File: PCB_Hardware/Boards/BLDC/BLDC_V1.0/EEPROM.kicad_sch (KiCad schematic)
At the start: 4 parts, among them U16 CAT24C256

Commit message: Add DBcan transport refactor, BLDC V1.0 schematic + sim work, HAL submodule
- DBcan: replace bare-register driver with vendor-agnostic transport abstraction (core/, transports/, refactored bootloader driver, README)
- Add stm32g4xx_hal_driver as Firmware/libs submodule
- Add HAL config for BLDC board (stm32g4xx_hal_conf.h)
- BLDC V1.0: schematic edits across 10 sheets (footprint assignments, repositioning); design-doc README (gate-driver constraints, FET selection / TPH3R70APL, thermal analysis)
- ngspice simulation workflow (cap sweeps, half-bridge slow turn-on)
- Ignore .obsidian/ vault state and large simulation CSV exports
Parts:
- C46: footprint (none) -> Capacitor_SMD:C_0402_1005Metric
- R27, R28: footprint (none) -> Resistor_SMD:R_0402_1005Metric
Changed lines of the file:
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@@
 			)
 		)
-		(property "Footprint" ""
+		(property "Footprint" "Resistor_SMD:R_0402_1005Metric"
 			(at 137.922 88.9 90)
 			(hide yes)
@@
 			)
 		)
-		(property "Footprint" ""
+		(property "Footprint" "Capacitor_SMD:C_0402_1005Metric"
 			(at 152.0952 92.71 0)
 			(hide yes)
@@
 			)
 		)
-		(property "Footprint" ""
+		(property "Footprint" "Resistor_SMD:R_0402_1005Metric"
 			(at 127.762 88.9 90)
 			(hide yes)

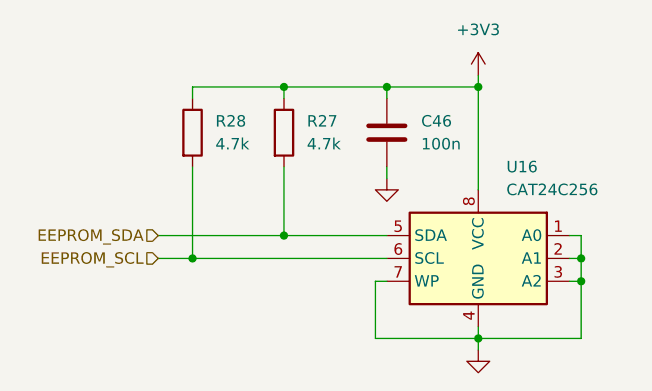
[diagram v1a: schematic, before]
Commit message: Created organization around the symbol lib and did a first pass layout of the BDLC
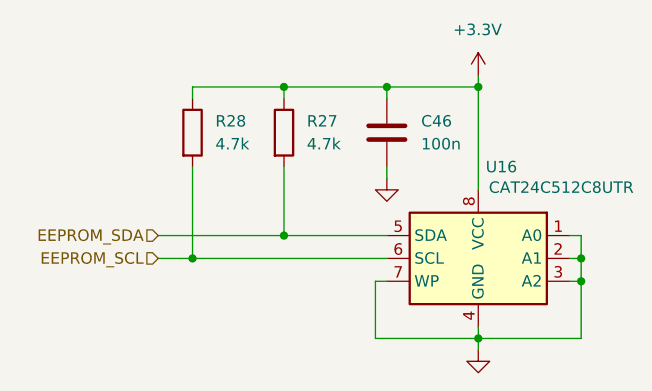
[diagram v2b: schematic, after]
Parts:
- U16: value CAT24C256 -> CAT24C512C8UTR; footprint (none) -> DBRobot:CAT24C512C8UTR
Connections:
- net +3V3 renamed +3.3V
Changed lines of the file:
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@@
-	)
-	(symbol
-		(lib_id "Memory_EEPROM:CAT24C256")
-		(at 161.29 102.87 0)
-		(mirror y)
-		(unit 1)
-		(body_style 1)
-		(exclude_from_sim no)
-		(in_bom yes)
-		(on_board yes)
-		(in_pos_files yes)
-		(dnp no)
-		(fields_autoplaced yes)
-		(property "Reference" "U16"
-			(at 164.4081 92.71 0)
-			(show_name no)
-			(do_not_autoplace no)
-			(effects
-				(font
-					(size 1.27 1.27)
-				)
-				(justify right)
-			)
-		)
-		(property "Value" "CAT24C256"
-			(at 164.4081 95.25 0)
-			(show_name no)
-			(do_not_autoplace no)
-			(effects
-				(font
-					(size 1.27 1.27)
-				)
-				(justify right)
-			)
-		)
-		(property "Footprint" ""
-			(at 161.29 102.87 0)
-			(hide yes)
-			(show_name no)
-			(do_not_autoplace no)
-			(effects
-				(font
-					(size 1.27 1.27)
-				)
-			)
-		)
-		(property "Datasheet" "https://www.onsemi.cn/PowerSolutions/document/CAT24C256-D.PDF"
-			(at 161.29 102.87 0)
-			(hide yes)
-			(show_name no)
-			(do_not_autoplace no)
-			(effects
-				(font
-					(size 1.27 1.27)
-				)
-			)
-		)
-		(property "Description" "256 kb CMOS Serial EEPROM, DIP-8/SOIC-8/TSSOP-8/DFN-8"
-			(at 161.29 102.87 0)
-			(hide yes)
-			(show_name no)
-			(do_not_autoplace no)
-			(effects
-				(font
-					(size 1.27 1.27)
-				)
-			)
-		)
-		(pin "3"
-		)
-		(pin "6"
-		)
-		(pin "1"
-		)
-		(pin "7"
-		)
-		(pin "5"
-		)
-		(pin "2"
-		)
-		(pin "4"
-		)
-		(pin "8"
-		)
-		(instances
-			(project "BLDC_V1.0"
-				(path "/55f9ea03-7b89-4b61-9599-7cac20295fbb/8c82480a-69eb-4e57-815e-68aa86fb6e72"
-					(reference "U16")
-					(unit 1)
-				)
-			)
-		)
 	)
 	(symbol
@@
 	)
 	(symbol
+		(lib_id "Memory_EEPROM:CAT24C256")
+		(at 161.29 102.87 0)
+		(mirror y)
+		(unit 1)
+		(body_style 1)
+		(exclude_from_sim no)
+		(in_bom yes)
+		(on_board yes)
+		(in_pos_files yes)
+		(dnp no)
+		(property "Reference" "U16"
+			(at 165.608 92.71 0)
+			(show_name no)
+			(do_not_autoplace no)
+			(effects
+				(font
+					(size 1.27 1.27)
+				)
+				(justify left)
+			)
+		)
+		(property "Value" "CAT24C512C8UTR"
+			(at 178.562 94.996 0)
+			(show_name no)
+			(do_not_autoplace no)
+			(effects
+				(font
+					(size 1.27 1.27)
+				)
+				(justify left)
+			)
+		)
+		(property "Footprint" "DBRobot:CAT24C512C8UTR"
+			(at 161.29 102.87 0)
+			(hide yes)
+			(show_name no)
+			(do_not_autoplace no)
+			(effects
+				(font
+					(size 1.27 1.27)
+				)
+			)
+		)
+		(property "Datasheet" "https://www.onsemi.cn/PowerSolutions/document/CAT24C256-D.PDF"
+			(at 161.29 102.87 0)
+			(hide yes)
+			(show_name no)
+			(do_not_autoplace no)
+			(effects
+				(font
+					(size 1.27 1.27)
+				)
+			)
+		)
+		(property "Description" "256 kb CMOS Serial EEPROM, DIP-8/SOIC-8/TSSOP-8/DFN-8"
+			(at 161.29 102.87 0)
+			(hide yes)
+			(show_name no)
+			(do_not_autoplace no)
+			(effects
+				(font
+					(size 1.27 1.27)
+				)
+			)
+		)
+		(pin "5"
+		)
+		(pin "4"
+		)
+		(pin "6"
+		)
+		(pin "7"
+		)
+		(pin "3"
+		)
+		(pin "1"
+		)
+		(pin "2"
+		)
+		(pin "8"
+		)
+		(instances
+			(project "BLDC_V1.0"
+				(path "/55f9ea03-7b89-4b61-9599-7cac20295fbb/8c82480a-69eb-4e57-815e-68aa86fb6e72"
+					(reference "U16")
+					(unit 1)
+				)
+			)
+		)
+	)
+	(symbol
 		(lib_id "power:+3V3")
 		(at 161.29 82.55 0)
@@
 		(in_pos_files yes)
 		(dnp no)
-		(fields_autoplaced yes)
 		(property "Reference" "#PWR068"
 			(at 161.29 86.36 0)
@@
 			)
 		)
-		(property "Value" "+3V3"
-			(at 161.29 77.47 0)
-			(show_name no)
-			(do_not_autoplace no)
-			(effects
-				(font
-					(size 1.27 1.27)
-				)
-			)
-		)
+		(property "Value" "+3.3V"
+			(at 158.496 77.47 0)
+			(show_name no)
+			(do_not_autoplace no)
+			(effects
+				(font
+					(size 1.27 1.27)
+				)
+				(justify left)
+			)
+		)
